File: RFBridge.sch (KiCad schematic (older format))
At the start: 0 parts

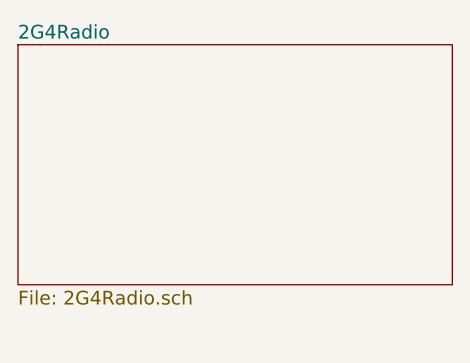
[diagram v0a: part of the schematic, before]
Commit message: added some radio components.
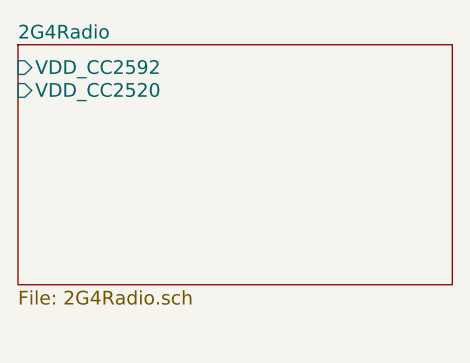
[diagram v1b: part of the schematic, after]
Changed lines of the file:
@@
 EESchema Schematic File Version 2
+LIBS:74xgxx
+LIBS:74xx
+LIBS:atmel
+LIBS:conn
+LIBS:dc-dc
 LIBS:Diodes
+LIBS:discrete_transistors
+LIBS:ftdi
+LIBS:interface
+LIBS:linear
+LIBS:memory
+LIBS:microcontrollers_dspic33dsc
+LIBS:microcontrollers_msp430
+LIBS:microcontrollers_pic10mcu
+LIBS:microcontrollers_pic12mcu
+LIBS:microcontrollers_pic16mcu
+LIBS:microcontrollers_pic18mcu
+LIBS:microcontrollers_pic32mcu
+LIBS:microcontrollers_stm8
+LIBS:microcontrollers_stm32
+LIBS:opto
 LIBS:Passives
+LIBS:power
+LIBS:regulators
+LIBS:sensors
+LIBS:switches
+LIBS:device
+LIBS:crystals_oscillators
+LIBS:misc
+LIBS:rf
 LIBS:RFBridge-cache
 EELAYER 25 0
@@
 F0 "2G4Radio" 60
 F1 "2G4Radio.sch" 60
+F2 "VDD_CC2592" I L 7800 1950 60
+F3 "VDD_CC2520" I L 7800 2050 60
 $EndSheet
 $Sheet

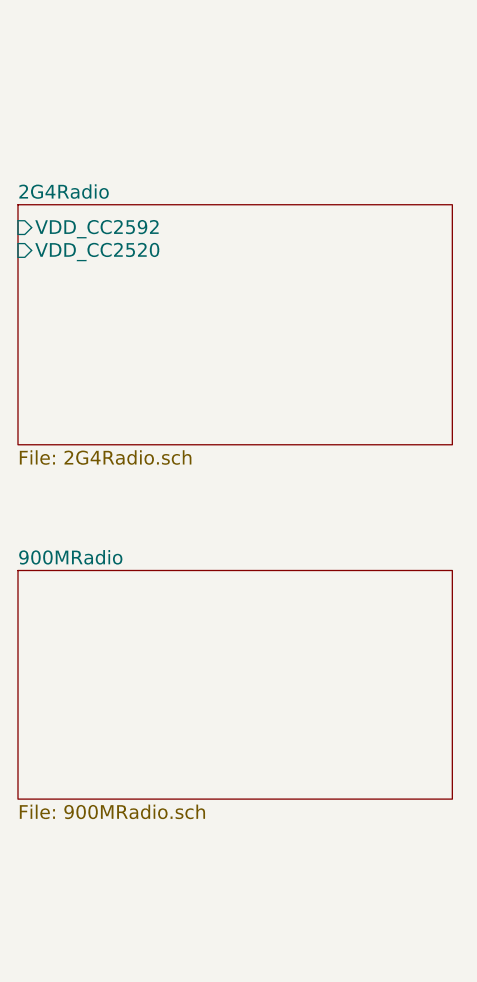
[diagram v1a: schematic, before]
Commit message: Finished schematic of 2.4GHz and 900MHz radios
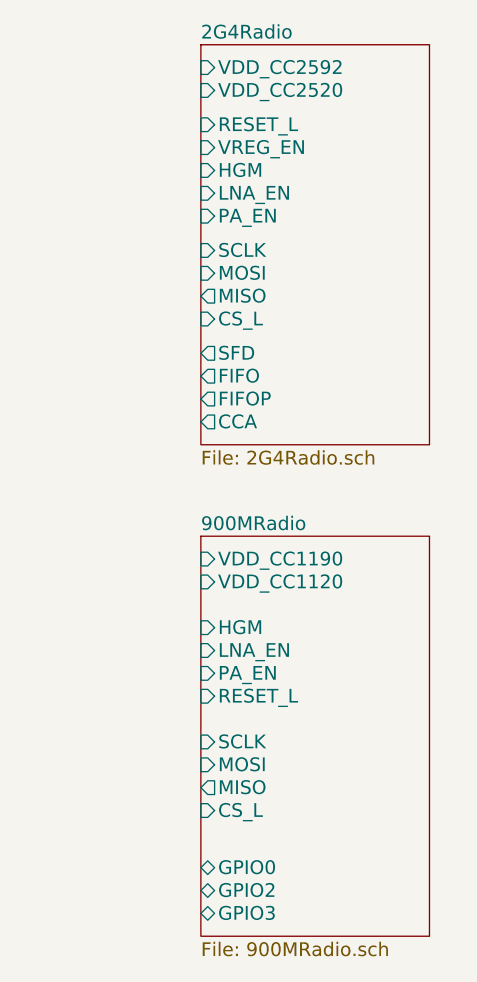
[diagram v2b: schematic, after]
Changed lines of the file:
@@
 LIBS:sensors
 LIBS:switches
-LIBS:device
 LIBS:crystals_oscillators
 LIBS:misc
@@
 $EndDescr
 $Sheet
-S 7800 1850 1900 1050
+S 8600 1150 1000 1750
 U 5597347E
 F0 "2G4Radio" 60
 F1 "2G4Radio.sch" 60
-F2 "VDD_CC2592" I L 7800 1950 60
-F3 "VDD_CC2520" I L 7800 2050 60
+F2 "VDD_CC2592" I L 8600 1250 60
+F3 "VDD_CC2520" I L 8600 1350 60
+F4 "MOSI" I L 8600 2150 60
+F5 "MISO" O L 8600 2250 60
+F6 "SCLK" I L 8600 2050 60
+F7 "RESET_L" I L 8600 1500 60
+F8 "VREG_EN" I L 8600 1600 60
+F9 "HGM" I L 8600 1700 60
+F10 "LNA_EN" I L 8600 1800 60
+F11 "PA_EN" I L 8600 1900 60
+F12 "SFD" O L 8600 2500 60
+F13 "FIFO" O L 8600 2600 60
+F14 "FIFOP" O L 8600 2700 60
+F15 "CCA" O L 8600 2800 60
+F16 "CS_L" I L 8600 2350 60
 $EndSheet
 $Sheet
-S 7800 3450 1900 1000
+S 8600 3300 1000 1750
 U 559734A3
 F0 "900MRadio" 60
 F1 "900MRadio.sch" 60
+F2 "HGM" I L 8600 3700 60
+F3 "LNA_EN" I L 8600 3800 60
+F4 "PA_EN" I L 8600 3900 60
+F5 "CS_L" I L 8600 4500 60
+F6 "MOSI" I L 8600 4300 60
+F7 "MISO" O L 8600 4400 60
+F8 "SCLK" I L 8600 4200 60
+F9 "RESET_L" I L 8600 4000 60
+F10 "VDD_CC1190" I L 8600 3400 60
+F11 "GPIO3" B L 8600 4950 60
+F12 "GPIO2" B L 8600 4850 60
+F13 "GPIO0" B L 8600 4750 60
+F14 "VDD_CC1120" I L 8600 3500 60
 $EndSheet
 $EndSCHEMATC

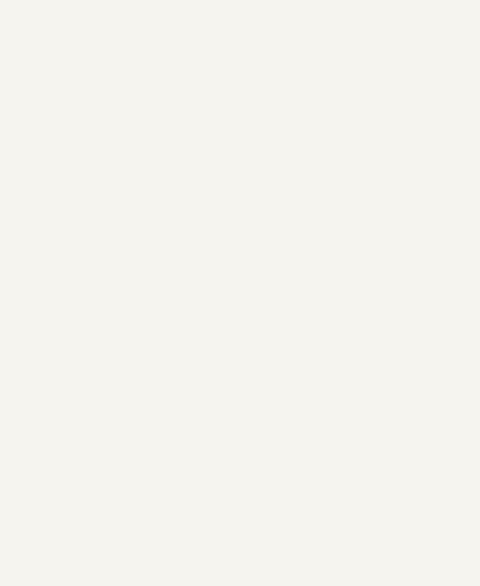
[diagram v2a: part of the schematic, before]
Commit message: Compressed design a bit.
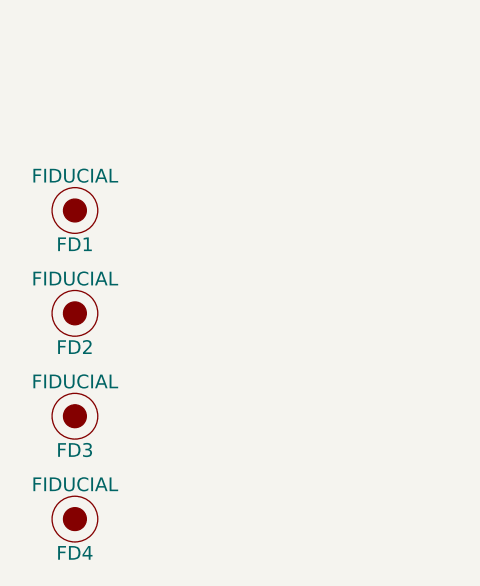
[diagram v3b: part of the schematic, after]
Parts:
- added FD1, FD2: FIDUCIAL, Fiducials:Fiducial_1mm_Dia_2.54mm_Outer_CopperBottom, symbol FIDUCIAL
- added FD3, FD4: FIDUCIAL, Fiducials:Fiducial_1mm_Dia_2.54mm_Outer_CopperTop, symbol FIDUCIAL
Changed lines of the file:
@@
 F14 "VDD_CC1120" I L 8600 3500 60
 $EndSheet
+$Comp
+L FIDUCIAL FD1
+U 1 1 55A304EC
+P 800 6100
+F 0 "FD1" H 800 5950 60  0000 C CNN
+F 1 "FIDUCIAL" H 800 6250 60  0000 C CNN
+F 2 "Fiducials:Fiducial_1mm_Dia_2.54mm_Outer_CopperBottom" H 800 6100 60  0001 C CNN
+F 3 "" H 800 6100 60  0000 C CNN
+	1    800  6100
+	1    0    0    -1
+$EndComp
+$Comp
+L FIDUCIAL FD2
+U 1 1 55A3092B
+P 800 6550
+F 0 "FD2" H 800 6400 60  0000 C CNN
+F 1 "FIDUCIAL" H 800 6700 60  0000 C CNN
+F 2 "Fiducials:Fiducial_1mm_Dia_2.54mm_Outer_CopperBottom" H 800 6550 60  0001 C CNN
+F 3 "" H 800 6550 60  0000 C CNN
+	1    800  6550
+	1    0    0    -1
+$EndComp
+$Comp
+L FIDUCIAL FD3
+U 1 1 55A30A11
+P 800 7000
+F 0 "FD3" H 800 6850 60  0000 C CNN
+F 1 "FIDUCIAL" H 800 7150 60  0000 C CNN
+F 2 "Fiducials:Fiducial_1mm_Dia_2.54mm_Outer_CopperTop" H 800 7000 60  0001 C CNN
+F 3 "" H 800 7000 60  0000 C CNN
+	1    800  7000
+	1    0    0    -1
+$EndComp
+$Comp
+L FIDUCIAL FD4
+U 1 1 55A30ADE
+P 800 7450
+F 0 "FD4" H 800 7300 60  0000 C CNN
+F 1 "FIDUCIAL" H 800 7600 60  0000 C CNN
+F 2 "Fiducials:Fiducial_1mm_Dia_2.54mm_Outer_CopperTop" H 800 7450 60  0001 C CNN
+F 3 "" H 800 7450 60  0000 C CNN
+	1    800  7450
+	1    0    0    -1
+$EndComp
 $EndSCHEMATC

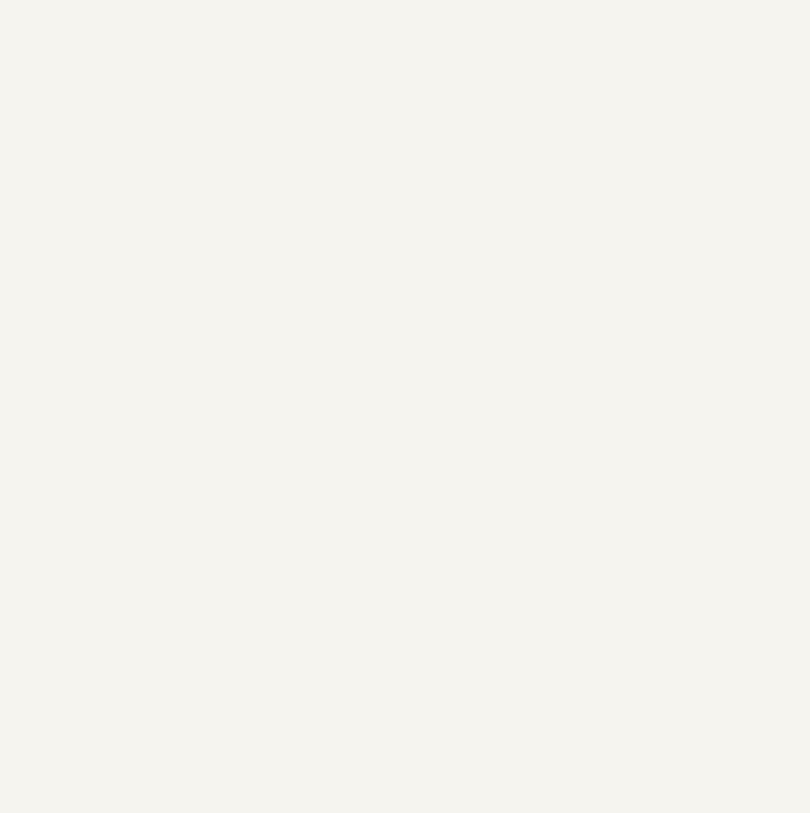
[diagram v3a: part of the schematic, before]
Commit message: Added XMC4500.sch
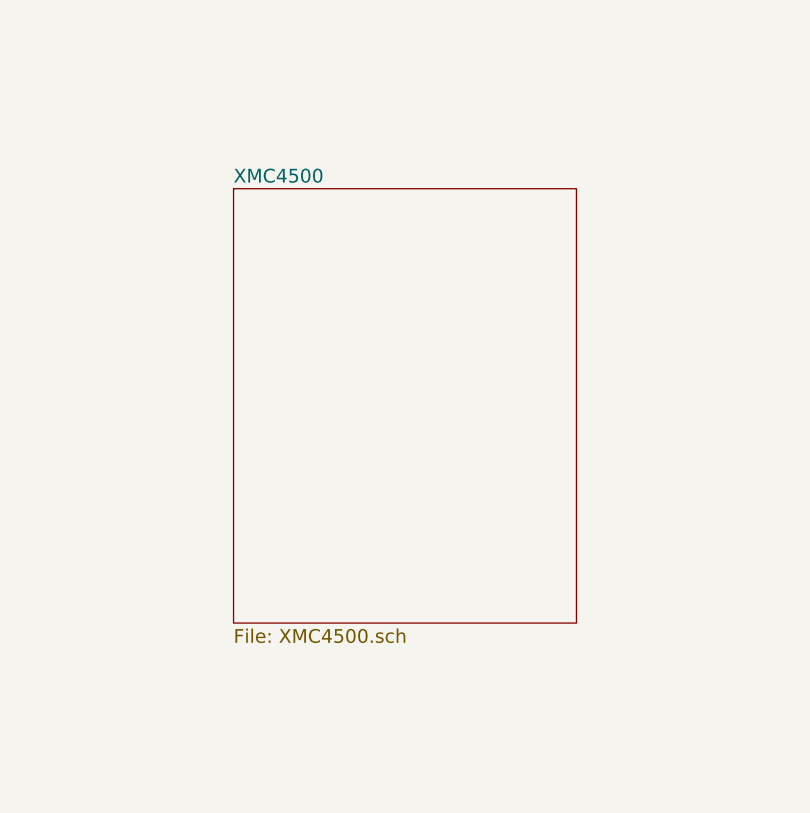
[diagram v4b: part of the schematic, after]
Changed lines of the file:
@@
 LIBS:misc
 LIBS:rf
+LIBS:microcontrollers_xmc
 LIBS:RFBridge-cache
 EELAYER 25 0
@@
 $Descr A4 11693 8268
 encoding utf-8
-Sheet 1 3
+Sheet 1 4
 Title ""
 Date ""
@@
 	1    0    0    -1
 $EndComp
+$Sheet
+S 3100 2650 1500 1900
+U 55B8AC40
+F0 "XMC4500" 60
+F1 "XMC4500.sch" 60
+$EndSheet
 $EndSCHEMATC

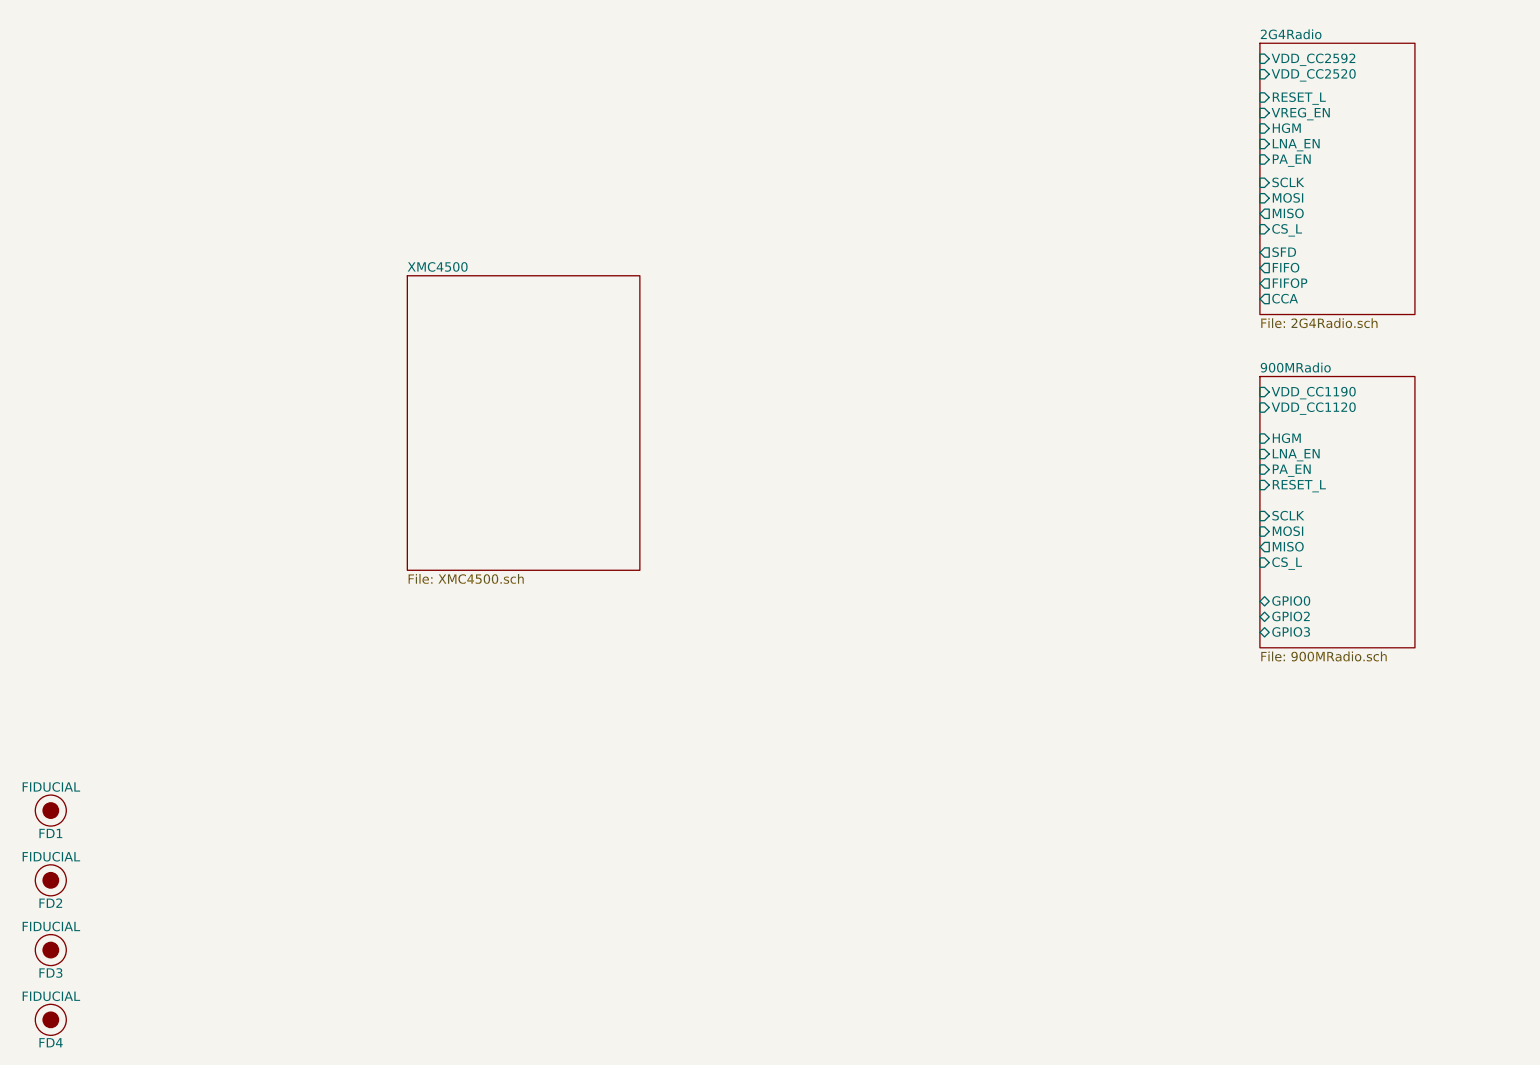
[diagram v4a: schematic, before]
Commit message: Added capacitors for XMC chip, diagram of power tree, and more connectors.
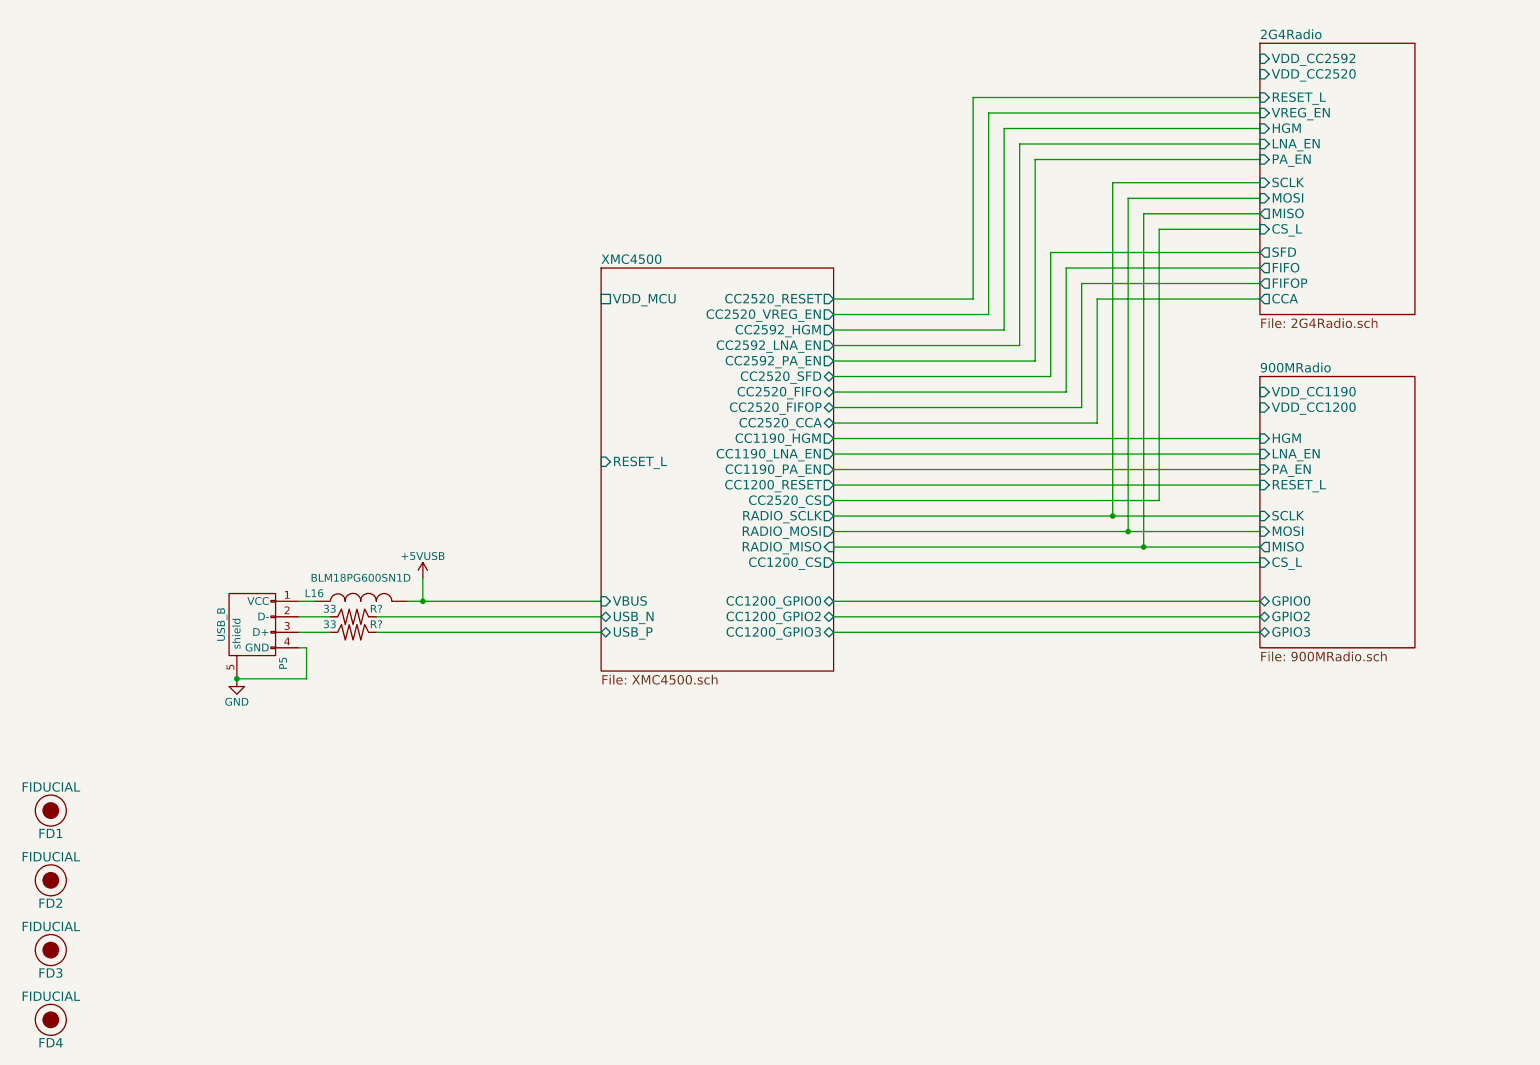
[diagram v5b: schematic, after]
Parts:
- added L16: BLM18PG600SN1D, Resistors_SMD:R_0603, symbol INDUCTOR
- added P5: USB_B, Connect:USB_Micro-B, symbol USB_B
- added R? (x2): 33, symbol R
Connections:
- new net: L16.1, P5.1 (VCC)
- new net: P5.2 (D-), R?.2
- new net: P5.3 (D+), R?.2
- new net +5VUSB: L16.2
- new net GND: P5.4 (GND), P5.5 (shield)
- new net XMC4500/USB_N: R?.1
- new net XMC4500/USB_P: R?.1
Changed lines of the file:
@@
 F12 "GPIO2" B L 8600 4850 60
 F13 "GPIO0" B L 8600 4750 60
-F14 "VDD_CC1120" I L 8600 3500 60
+F14 "VDD_CC1200" I L 8600 3500 60
 $EndSheet
 $Comp
@@
 $EndComp
 $Sheet
-S 3100 2650 1500 1900
+S 4350 2600 1500 2600
 U 55B8AC40
 F0 "XMC4500" 60
 F1 "XMC4500.sch" 60
+F2 "USB_P" B L 4350 4950 60
+F3 "USB_N" B L 4350 4850 60
+F4 "VBUS" I L 4350 4750 60
+F5 "RESET_L" I L 4350 3850 60
+F6 "VDD_MCU" U L 4350 2800 60
+F7 "RADIO_SCLK" O R 5850 4200 60
+F8 "RADIO_MOSI" O R 5850 4300 60
+F9 "RADIO_MISO" I R 5850 4400 60
+F10 "CC1200_CS" O R 5850 4500 60
+F11 "CC2520_CS" O R 5850 4100 60
+F12 "CC1190_HGM" O R 5850 3700 60
+F13 "CC1190_LNA_EN" O R 5850 3800 60
+F14 "CC1190_PA_EN" O R 5850 3900 60
+F15 "CC1200_GPIO0" B R 5850 4750 60
+F16 "CC1200_GPIO2" B R 5850 4850 60
+F17 "CC2520_FIFOP" B R 5850 3500 60
+F18 "CC2520_FIFO" B R 5850 3400 60
+F19 "CC2520_SFD" B R 5850 3300 60
+F20 "CC2592_PA_EN" O R 5850 3200 60
+F21 "CC2592_LNA_EN" O R 5850 3100 60
+F22 "CC2592_HGM" O R 5850 3000 60
+F23 "CC2520_VREG_EN" O R 5850 2900 60
+F24 "CC2520_RESET" O R 5850 2800 60
+F25 "CC1200_RESET" O R 5850 4000 60
+F26 "CC1200_GPIO3" B R 5850 4950 60
+F27 "CC2520_CCA" B R 5850 3600 60
 $EndSheet
+$Comp
+L USB_B P5
+U 1 1 55BFC1E8
+P 2100 4950
+F 0 "P5" H 2300 4750 50  0000 C CNN
+F 1 "USB_B" H 2050 5150 50  0000 C CNN
+F 2 "Connect:USB_Micro-B" V 2050 4850 60  0001 C CNN
+F 3 "" V 2050 4850 60  0000 C CNN
+	1    2100 4950
+	0    -1   1    0
+$EndComp
+Wire Wire Line
+	5850 4500 8600 4500
+Wire Wire Line
+	5850 4400 8600 4400
+Wire Wire Line
+	5850 4300 8600 4300
+Wire Wire Line
+	5850 4200 8600 4200
+Wire Wire Line
+	5850 4100 7950 4100
+Wire Wire Line
+	7950 4100 7950 2350
+Wire Wire Line
+	7950 2350 8600 2350
+Wire Wire Line
+	5850 4000 8600 4000
+Wire Wire Line
+	8600 3900 5850 3900
+Wire Wire Line
+	5850 3800 8600 3800
+Wire Wire Line
+	8600 3700 5850 3700
+Wire Wire Line
+	7850 2250 8600 2250
+Wire Wire Line
+	7850 2250 7850 4400
+Connection ~ 7850 4400
+Wire Wire Line
+	7750 4300 7750 2150
+Wire Wire Line
+	7750 2150 8600 2150
+Connection ~ 7750 4300
+Wire Wire Line
+	8600 2050 7650 2050
+Wire Wire Line
+	7650 2050 7650 4200
+Connection ~ 7650 4200
+Wire Wire Line
+	5850 4750 8600 4750
+Wire Wire Line
+	8600 4850 5850 4850
+Wire Wire Line
+	5850 4950 8600 4950
+Wire Wire Line
+	5850 3600 7550 3600
+Wire Wire Line
+	7550 3600 7550 2800
+Wire Wire Line
+	7550 2800 8600 2800
+Wire Wire Line
+	8600 2700 7450 2700
+Wire Wire Line
+	7450 2700 7450 3500
+Wire Wire Line
+	7450 3500 5850 3500
+Wire Wire Line
+	5850 3400 7350 3400
+Wire Wire Line
+	7350 3400 7350 2600
+Wire Wire Line
+	7350 2600 8600 2600
+Wire Wire Line
+	8600 2500 7250 2500
+Wire Wire Line
+	7250 2500 7250 3300
+Wire Wire Line
+	7250 3300 5850 3300
+Wire Wire Line
+	5850 3200 7150 3200
+Wire Wire Line
+	7150 3200 7150 1900
+Wire Wire Line
+	7150 1900 8600 1900
+Wire Wire Line
+	8600 1800 7050 1800
+Wire Wire Line
+	7050 1800 7050 3100
+Wire Wire Line
+	7050 3100 5850 3100
+Wire Wire Line
+	5850 3000 6950 3000
+Wire Wire Line
+	6950 3000 6950 1700
+Wire Wire Line
+	6950 1700 8600 1700
+Wire Wire Line
+	8600 1600 6850 1600
+Wire Wire Line
+	6850 1600 6850 2900
+Wire Wire Line
+	6850 2900 5850 2900
+Wire Wire Line
+	5850 2800 6750 2800
+Wire Wire Line
+	6750 2800 6750 1500
+Wire Wire Line
+	6750 1500 8600 1500
+Wire Wire Line
+	2400 5050 2450 5050
+Wire Wire Line
+	2450 5050 2450 5250
+Wire Wire Line
+	2450 5250 2000 5250
+Connection ~ 2000 5250
+$Comp
+L GND #PWR1
+U 1 1 55C0146A
+P 2000 5250
+F 0 "#PWR1" H 2000 5000 50  0001 C CNN
+F 1 "GND" H 2000 5100 50  0000 C CNN
+F 2 "" H 2000 5250 60  0000 C CNN
+F 3 "" H 2000 5250 60  0000 C CNN
+	1    2000 5250
+	1    0    0    -1
+$EndComp
+$Comp
+L +5VUSB #PWR2
+U 1 1 55C065DE
+P 3200 4600
+F 0 "#PWR2" H 3200 4450 50  0001 C CNN
+F 1 "+5VUSB" H 3200 4740 50  0000 C CNN
+F 2 "" H 3200 4600 60  0000 C CNN
+F 3 "" H 3200 4600 60  0000 C CNN
+	1    3200 4600
+	1    0    0    -1
+$EndComp
+Wire Wire Line
+	3100 4750 4350 4750
+$Comp
+L INDUCTOR L16
+U 1 1 55C07755
+P 2800 4750
+F 0 "L16" V 2850 5050 50  0000 C CNN
+F 1 "BLM18PG600SN1D" V 2950 4750 50  0000 C CNN
+F 2 "Resistors_SMD:R_0603" H 2800 4750 60  0001 C CNN
+F 3 "" H 2800 4750 60  0000 C CNN
+	1    2800 4750
+	0    -1   -1   0
+$EndComp
+Wire Wire Line
+	2400 4750 2500 4750
+Wire Wire Line
+	3200 4750 3200 4600
+Connection ~ 3200 4750
+$Comp
+L R R?
+U 1 1 55C0AB1C
+P 2750 4850
+F 0 "R?" V 2700 5000 50  0000 C CNN
+F 1 "33" V 2700 4700 50  0000 C CNN
+F 2 "" V 2680 4850 30  0000 C CNN
+F 3 "" H 2750 4850 30  0000 C CNN
+	1    2750 4850
+	0    1    1    0
+$EndComp
+$Comp
+L R R?
+U 1 1 55C0B00E
+P 2750 4950
+F 0 "R?" V 2700 5100 50  0000 C CNN
+F 1 "33" V 2700 4800 50  0000 C CNN
+F 2 "" V 2680 4950 30  0000 C CNN
+F 3 "" H 2750 4950 30  0000 C CNN
+	1    2750 4950
+	0    1    1    0
+$EndComp
+Wire Wire Line
+	2400 4850 2600 4850
+Wire Wire Line
+	2400 4950 2600 4950
+Wire Wire Line
+	4350 4850 2900 4850
+Wire Wire Line
+	2900 4950 4350 4950
 $EndSCHEMATC
